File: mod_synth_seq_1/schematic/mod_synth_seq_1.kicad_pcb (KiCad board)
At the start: 2 copper layers, 38.1 x 109.2 mm, 38 parts, among them J1 CV1, J10 Reset, J11 Clock, J2 Step 1 Gate, J3 Step 2 Gate, J4 Step 3 Gate, J5 Step 4 Gate, J6 Conn_02x08_Odd_Even

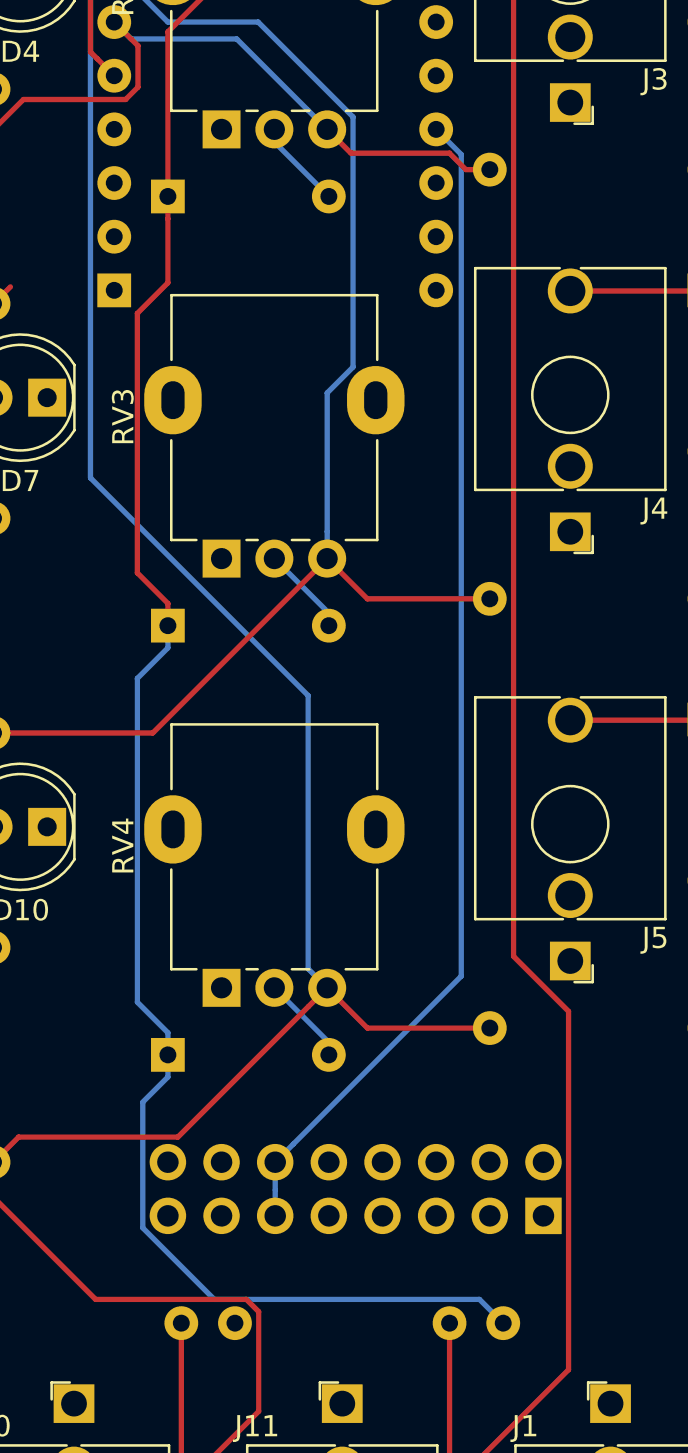
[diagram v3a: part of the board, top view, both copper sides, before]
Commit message: Centre connector, add arduino code
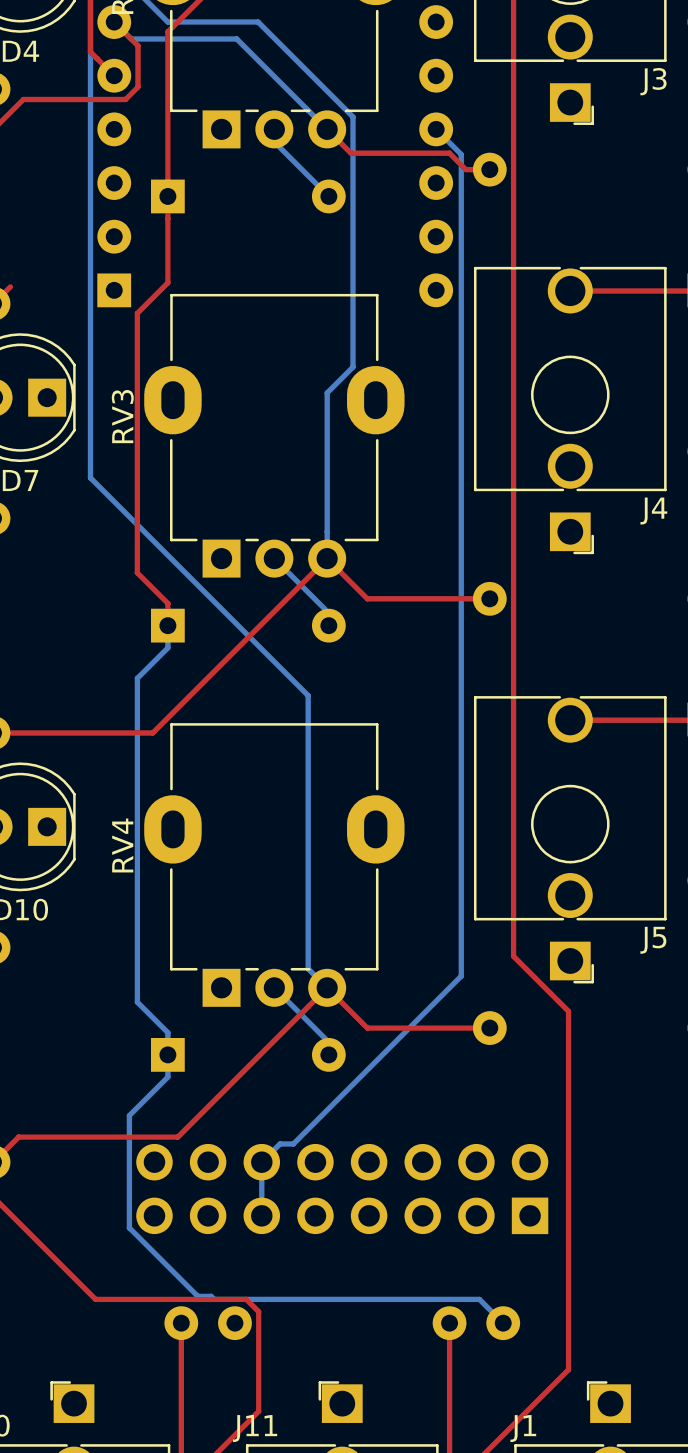
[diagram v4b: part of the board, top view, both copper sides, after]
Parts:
- moved J6 0.64 mm to (91.4, 105.4)
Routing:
- net Net-(D11-Pad1): track 92.6 -> 93.5 mm
- net +5V: track 55.6 -> 56.2 mm
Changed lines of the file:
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@@
     (thickness 1.6)
     (drawings 4)
-    (tracks 136)
+    (tracks 138)
     (zones 0)
     (modules 38)
@@
   (page A4)
   (layers
-    (0 F.Cu signal)
+    (0 F.Cu signal hide)
     (31 B.Cu signal)
     (32 B.Adhes user)
@@
   )
   (module Connector_IDC:IDC-Header_2x08_P2.54mm_Vertical (layer B.Cu)
-    (at 92.075 105.41 90)
+    (at 91.44 105.41 90)
     (descr "Through hole straight IDC box header, 2x08, 2.54mm pitch, double rows")
     (tags "Through hole IDC box header THT 2x08 2.54mm double row")
@@
   (segment (start 78.595001 114.664999) (end 76.2 117.06) (width 0.25) (layer F.Cu) (net 4))
   (segment (start 71.755 28.575) (end 64.77 35.56) (width 0.25) (layer F.Cu) (net 4))
-  (segment (start 80.238599 102.006401) (end 79.375 102.87) (width 0.25) (layer B.Cu) (net 9))
-  (segment (start 88.183601 94.061399) (end 80.238599 102.006401) (width 0.25) (layer B.Cu) (net 9))
-  (segment (start 88.183601 55.163601) (end 88.183601 94.061399) (width 0.25) (layer B.Cu) (net 9))
-  (segment (start 86.995 53.975) (end 88.183601 55.163601) (width 0.25) (layer B.Cu) (net 9))
-  (segment (start 79.375 104.188686) (end 79.375 102.87) (width 0.25) (layer B.Cu) (net 9))
-  (segment (start 79.375 105.41) (end 79.375 104.188686) (width 0.25) (layer B.Cu) (net 9))
+  (segment (start 78.74 105.41) (end 78.74 102.87) (width 0.25) (layer B.Cu) (net 9))
+  (segment (start 88.183601 55.163601) (end 86.995 53.975) (width 0.25) (layer B.Cu) (net 9))
+  (segment (start 88.183601 94.061399) (end 88.183601 55.163601) (width 0.25) (layer B.Cu) (net 9))
+  (segment (start 80.238599 102.006401) (end 88.183601 94.061399) (width 0.25) (layer B.Cu) (net 9))
+  (segment (start 79.603599 102.006401) (end 80.238599 102.006401) (width 0.25) (layer B.Cu) (net 9))
+  (segment (start 78.74 102.87) (end 79.603599 102.006401) (width 0.25) (layer B.Cu) (net 9))
   (segment (start 83.74 96.52) (end 88.9 96.52) (width 0.25) (layer F.Cu) (net 16))
   (segment (start 81.835 94.615) (end 83.74 96.52) (width 0.25) (layer F.Cu) (net 16))
@@
   (segment (start 81.915 36.235) (end 81.915 36.83) (width 0.25) (layer B.Cu) (net 32))
   (segment (start 79.335 33.655) (end 81.915 36.235) (width 0.25) (layer B.Cu) (net 32))
-  (segment (start 74.295 98.84) (end 74.295 97.79) (width 0.25) (layer B.Cu) (net 33))
-  (segment (start 73.106399 100.028601) (end 74.295 98.84) (width 0.25) (layer B.Cu) (net 33))
-  (segment (start 73.106399 105.980529) (end 73.106399 100.028601) (width 0.25) (layer B.Cu) (net 33))
-  (segment (start 76.490869 109.364999) (end 73.106399 105.980529) (width 0.25) (layer B.Cu) (net 33))
-  (segment (start 89.044999 109.364999) (end 76.490869 109.364999) (width 0.25) (layer B.Cu) (net 33))
-  (segment (start 90.17 110.49) (end 89.044999 109.364999) (width 0.25) (layer B.Cu) (net 33))
   (segment (start 74.295 78.52) (end 74.295 77.47) (width 0.25) (layer B.Cu) (net 33))
   (segment (start 72.84999 79.96501) (end 74.295 78.52) (width 0.25) (layer B.Cu) (net 33))
@@
   (segment (start 74.295 49.357963) (end 76.22001 47.432953) (width 0.25) (layer F.Cu) (net 33))
   (segment (start 74.295 57.15) (end 74.295 49.357963) (width 0.25) (layer F.Cu) (net 33))
+  (segment (start 89.044999 109.364999) (end 90.17 110.49) (width 0.25) (layer B.Cu) (net 33))
+  (segment (start 76.490869 109.364999) (end 89.044999 109.364999) (width 0.25) (layer B.Cu) (net 33))
+  (segment (start 74.295 98.84) (end 72.471399 100.663601) (width 0.25) (layer B.Cu) (net 33))
+  (segment (start 74.295 97.79) (end 74.295 98.84) (width 0.25) (layer B.Cu) (net 33))
+  (segment (start 72.471399 100.663601) (end 72.471399 105.980529) (width 0.25) (layer B.Cu) (net 33))
+  (segment (start 72.471399 105.980529) (end 75.71087 109.22) (width 0.25) (layer B.Cu) (net 33))
+  (segment (start 75.71087 109.22) (end 76.34587 109.22) (width 0.25) (layer B.Cu) (net 33))
+  (segment (start 76.34587 109.22) (end 76.490869 109.364999) (width 0.25) (layer B.Cu) (net 33))
   (segment (start 99.695 28.575) (end 99.695 35.56) (width 0.25) (layer F.Cu) (net 34))
   (segment (start 99.665 20.985) (end 99.695 20.955) (width 0.25) (layer F.Cu) (net 35))

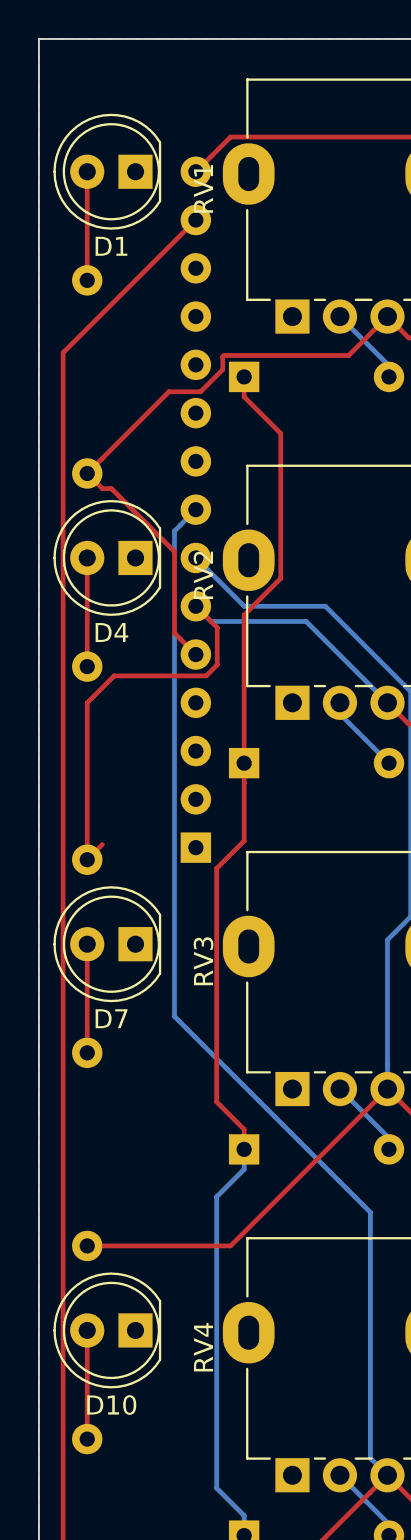
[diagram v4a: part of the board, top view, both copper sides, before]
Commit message: Move LEDs
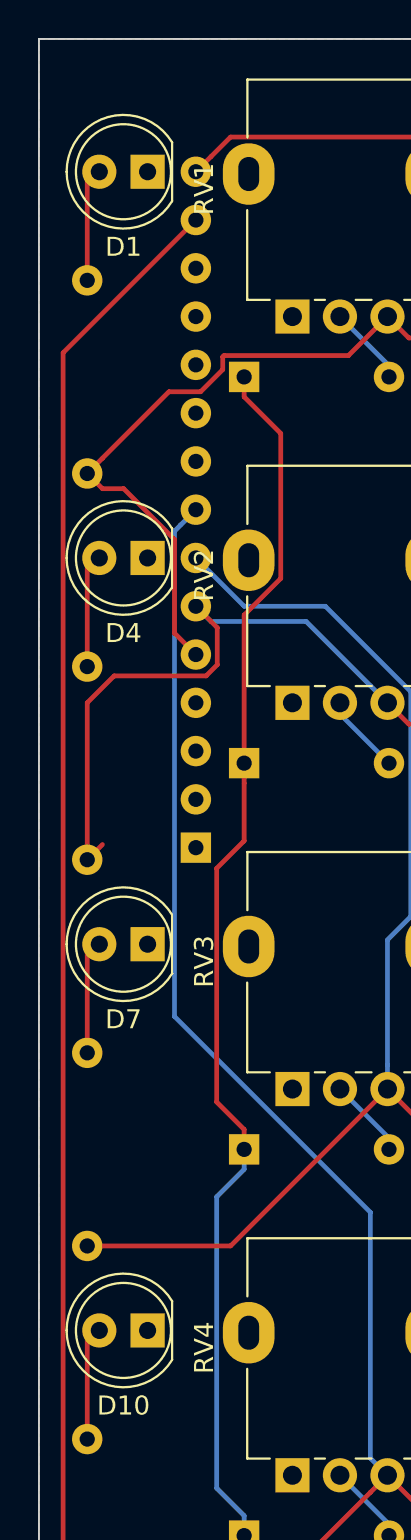
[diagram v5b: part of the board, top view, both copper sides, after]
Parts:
- moved D1 0.64 mm to (69.2, 26.0)
- moved D10 0.64 mm to (69.2, 87.0)
- moved D4 0.64 mm to (69.2, 46.4)
- moved D7 0.64 mm to (69.2, 66.7)

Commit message: Change potentiometer pads
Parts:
- RV1, RV2, RV3, RV4: footprint Potentiometer_THT:Potentiometer_Alpha_RD901F-40-00D_Single_Vertical -> Potentiometer_THT:Potentiometer_Alpha_RD901F-40-00D_Single_Vertical_CircularHoles
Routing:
- net Net-(D11-Pad1): track 93.5 -> 94.1 mm
